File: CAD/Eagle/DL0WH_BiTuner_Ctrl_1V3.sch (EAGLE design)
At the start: 159 parts, among them Q0321 ABS07-32.768KHZ, U0101 STM32L476RGT6_64PIN_LDO, U0601 MC33996, U0701 MC33996, U0801 MC33996, U0921 TS5A23166, U0941 LM2611, U0951 OPA354, U0961 OPA354, U0962 MCP4661-103E-MS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

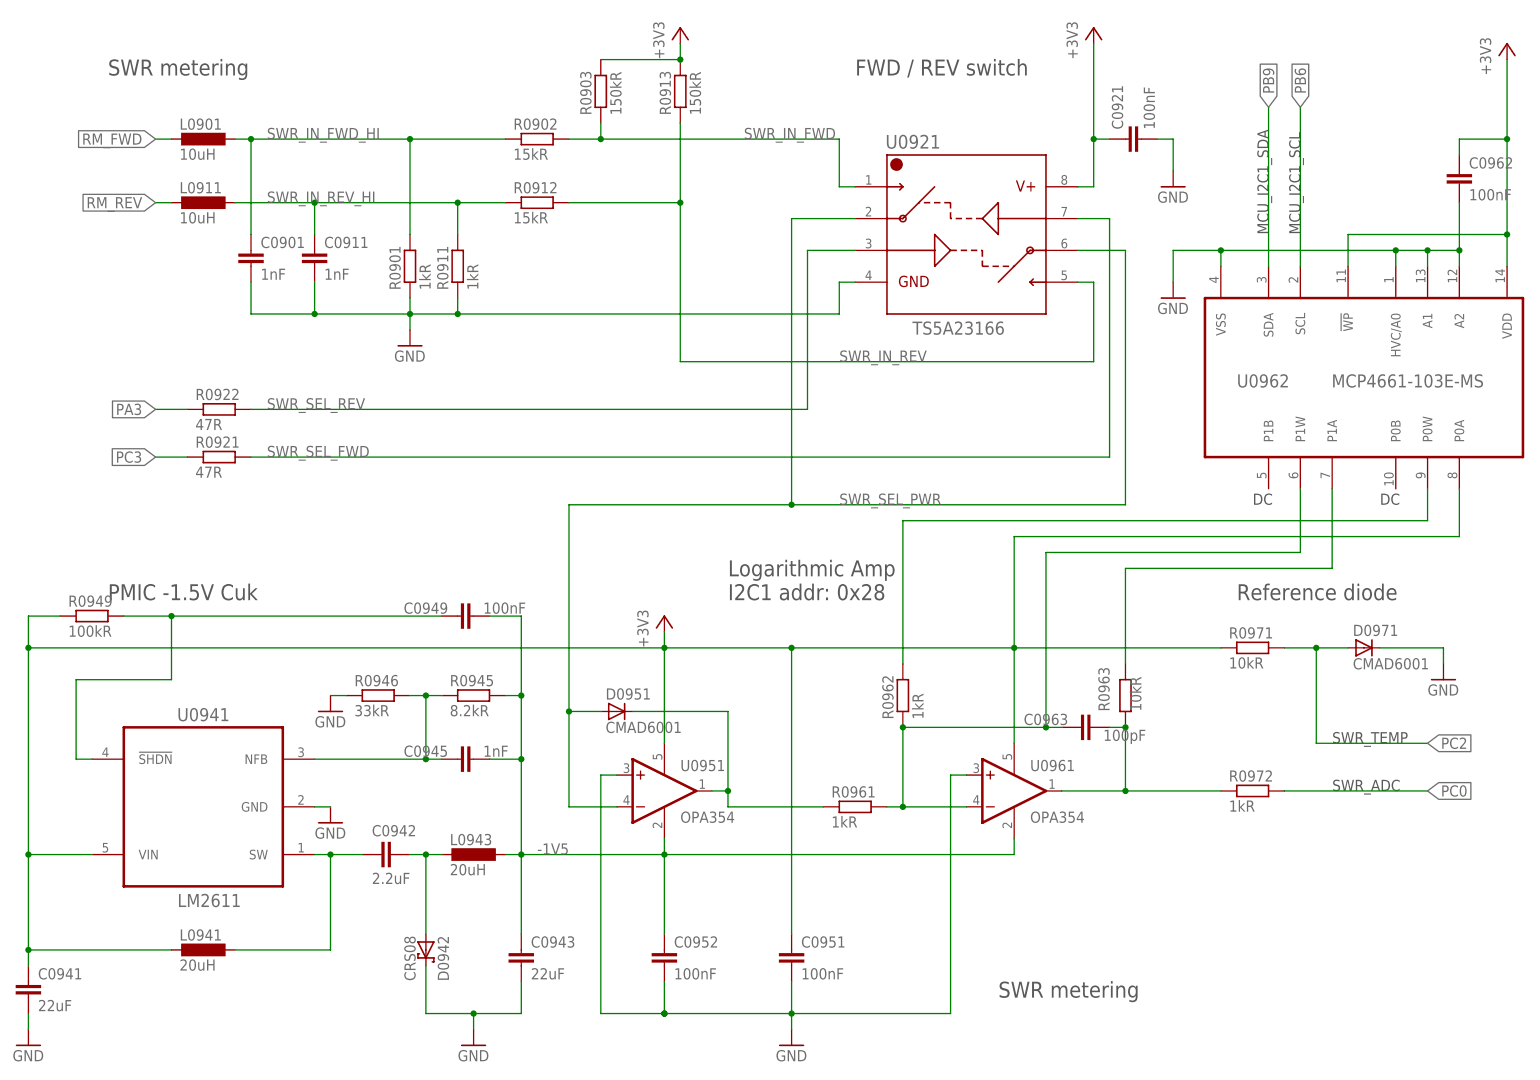
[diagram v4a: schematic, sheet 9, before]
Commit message: HW_1V3 - CAD/Eagle - soft-start not neded, prog. potis nominal values added
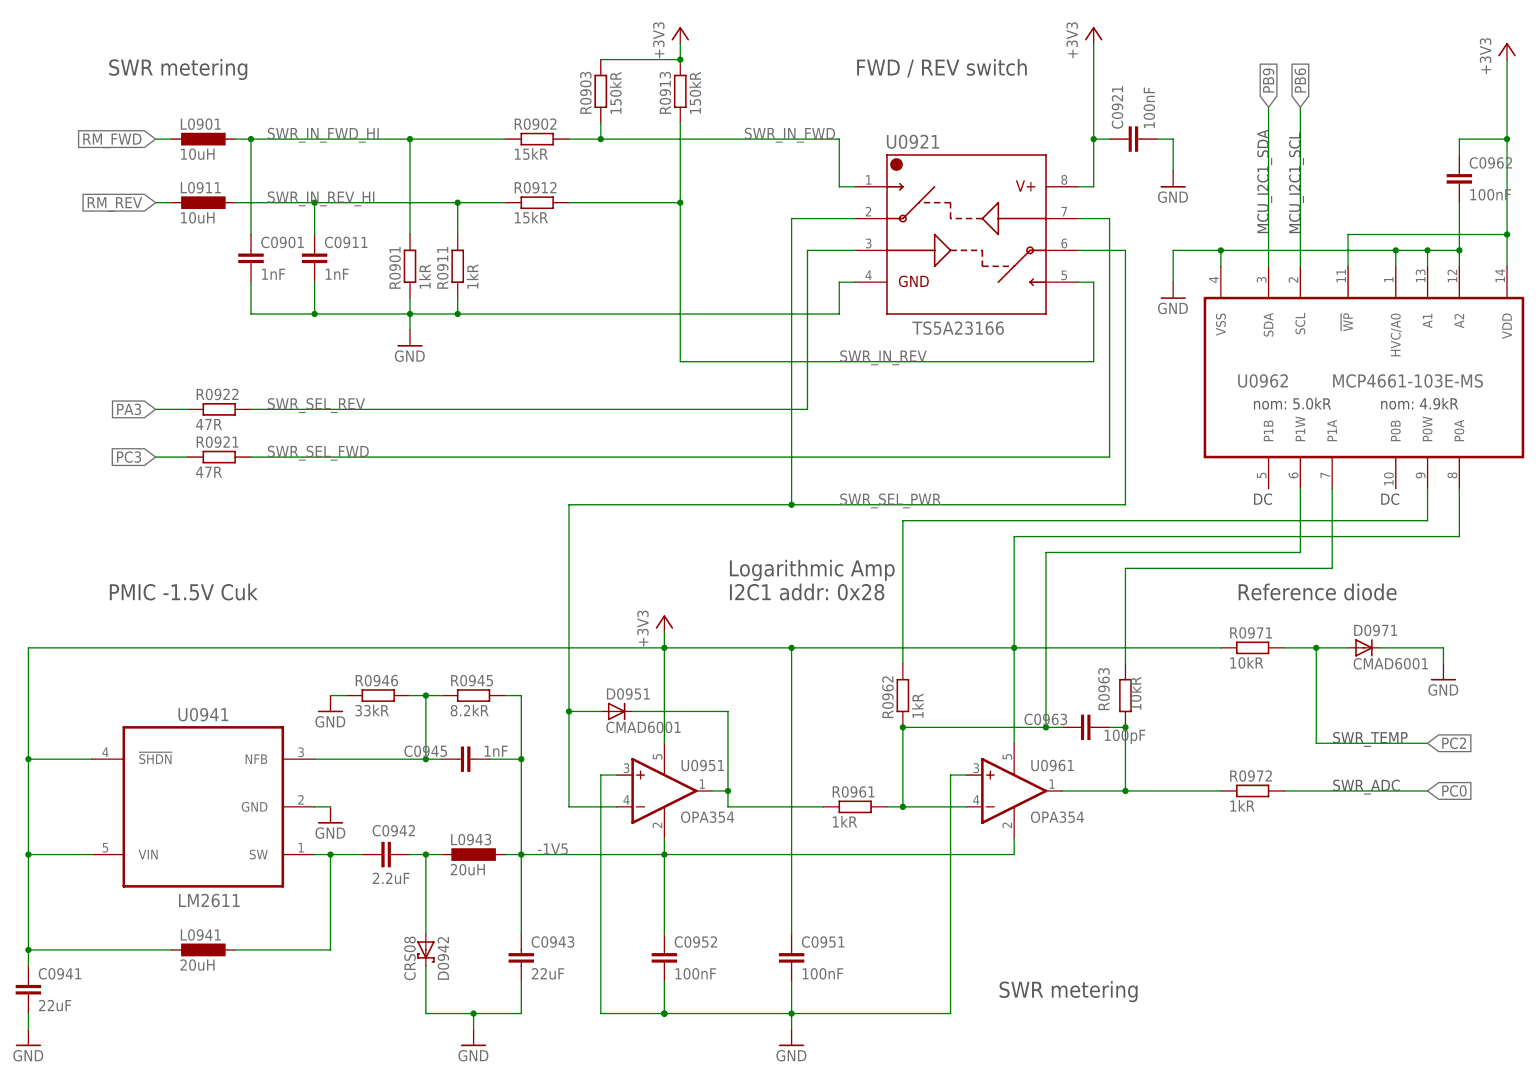
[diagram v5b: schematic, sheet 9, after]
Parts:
- removed C0949: 100nF, df4iah_rcl:C-EUC0402
- removed R0949: 100kR, df4iah_rcl:R-EU_R0402
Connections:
- removed net LM_SHDN: C0949.1, R0949.2, U0941.!SHDN
- net +3V3: now also U0941.!SHDN; no longer R0949.1
- net -1V5: no longer C0949.2
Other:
- note added: "nom: 4.9kR"
- note added: "nom: 5.0kR"
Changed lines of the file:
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@@
 <part name="+3V7" library="df4iah_supply" deviceset="+3V3" device=""/>
 <part name="C0962" library="df4iah_rcl" deviceset="C-EU" device="C0402" value="100nF"/>
-<part name="C0949" library="df4iah_rcl" deviceset="C-EU" device="C0402" value="100nF"/>
-<part name="R0949" library="df4iah_rcl" deviceset="R-EU_" device="R0402" value="100kR"/>
 </parts>
 <sheets>
@@
 <text x="213.36" y="137.16" size="1.778" layer="97" rot="R90">MCU_I2C1_SCL</text>
 <text x="208.28" y="137.16" size="1.778" layer="97" rot="R90">MCU_I2C1_SDA</text>
+<text x="205.74" y="109.22" size="1.778" layer="97">nom: 5.0kR</text>
+<text x="226.06" y="109.22" size="1.778" layer="97">nom: 4.9kR</text>
 </plain>
 <instances>
@@
 <instance part="+3V7" gate="G$1" x="246.38" y="167.64"/>
 <instance part="C0962" gate="G$1" x="238.76" y="147.32"/>
-<instance part="C0949" gate="G$1" x="78.74" y="76.2" smashed="yes" rot="R90">
-<attribute name="NAME" x="70.104" y="76.581" size="1.778" layer="95"/>
-<attribute name="VALUE" x="82.804" y="76.581" size="1.778" layer="96"/>
-</instance>
-<instance part="R0949" gate="G$1" x="20.32" y="76.2"/>
 </instances>
 <busses>
@@
 <pinref part="U0941" gate="G$1" pin="VIN"/>
 <wire x1="20.32" y1="38.1" x2="10.16" y2="38.1" width="0.1524" layer="91"/>
-<wire x1="10.16" y1="71.12" x2="10.16" y2="38.1" width="0.1524" layer="91"/>
+<wire x1="10.16" y1="71.12" x2="10.16" y2="53.34" width="0.1524" layer="91"/>
 <pinref part="C0941" gate="G$1" pin="1"/>
+<wire x1="10.16" y1="53.34" x2="10.16" y2="38.1" width="0.1524" layer="91"/>
 <wire x1="10.16" y1="38.1" x2="10.16" y2="22.86" width="0.1524" layer="91"/>
 <junction x="10.16" y="38.1"/>
@@
 <pinref part="U0962" gate="G$1" pin="P0A"/>
 <wire x1="238.76" y1="88.9" x2="238.76" y2="96.52" width="0.1524" layer="91"/>
-<wire x1="10.16" y1="71.12" x2="10.16" y2="76.2" width="0.1524" layer="91"/>
-<junction x="10.16" y="71.12"/>
-<pinref part="R0949" gate="G$1" pin="1"/>
-<wire x1="10.16" y1="76.2" x2="15.24" y2="76.2" width="0.1524" layer="91"/>
+<pinref part="U0941" gate="G$1" pin="!SHDN"/>
+<wire x1="10.16" y1="53.34" x2="20.32" y2="53.34" width="0.1524" layer="91"/>
+<junction x="10.16" y="53.34"/>
 </segment>
 <segment>
@@
 <wire x1="88.9" y1="53.34" x2="83.82" y2="53.34" width="0.1524" layer="91"/>
 <junction x="88.9" y="53.34"/>
-<wire x1="88.9" y1="63.5" x2="88.9" y2="76.2" width="0.1524" layer="91"/>
-<junction x="88.9" y="63.5"/>
-<pinref part="C0949" gate="G$1" pin="2"/>
-<wire x1="88.9" y1="76.2" x2="83.82" y2="76.2" width="0.1524" layer="91"/>
 </segment>
 </net>
@@
 </segment>
 </net>
-<net name="LM_SHDN" class="0">
-<segment>
-<pinref part="U0941" gate="G$1" pin="!SHDN"/>
-<wire x1="20.32" y1="53.34" x2="17.78" y2="53.34" width="0.1524" layer="91"/>
-<wire x1="17.78" y1="53.34" x2="17.78" y2="66.04" width="0.1524" layer="91"/>
-<wire x1="17.78" y1="66.04" x2="33.02" y2="66.04" width="0.1524" layer="91"/>
-<wire x1="33.02" y1="66.04" x2="33.02" y2="76.2" width="0.1524" layer="91"/>
-<pinref part="R0949" gate="G$1" pin="2"/>
-<wire x1="33.02" y1="76.2" x2="25.4" y2="76.2" width="0.1524" layer="91"/>
-<pinref part="C0949" gate="G$1" pin="1"/>
-<wire x1="33.02" y1="76.2" x2="76.2" y2="76.2" width="0.1524" layer="91"/>
-<junction x="33.02" y="76.2"/>
-</segment>
-</net>

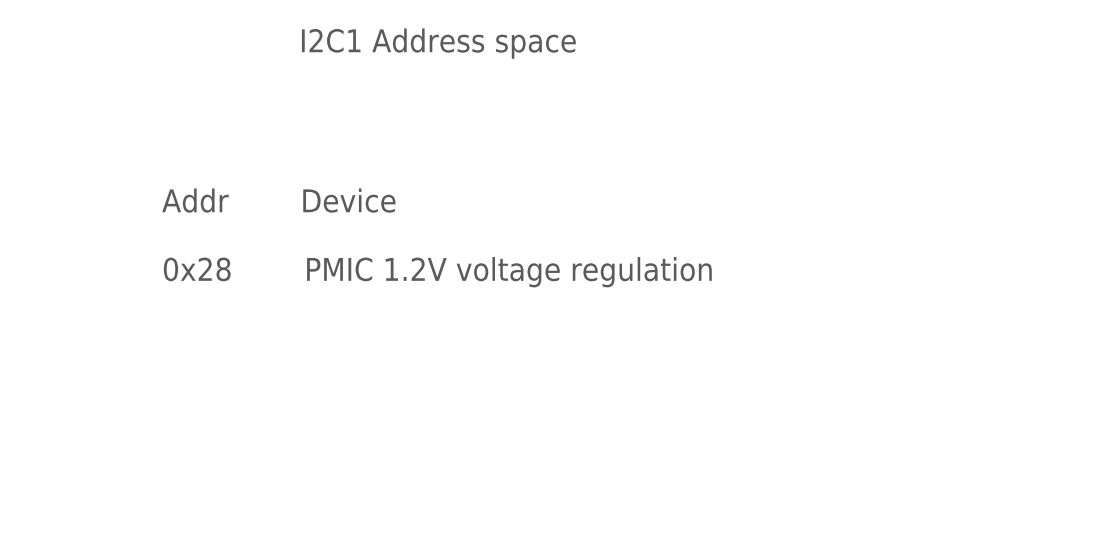
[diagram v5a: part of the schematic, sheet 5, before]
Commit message: HW_1V3 - CAD/Eagle - I2C address of dig.poti fixed to 0x14
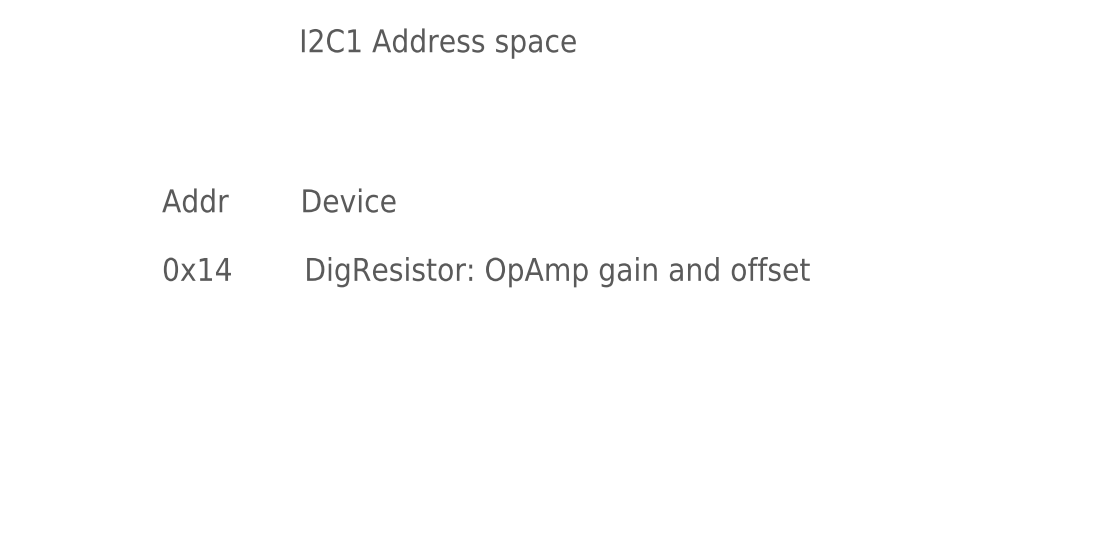
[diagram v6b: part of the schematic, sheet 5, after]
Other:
- note added: "Addr Device 0x14 DigResistor: OpAmp gain and offset"
- note removed: "Addr Device 0x28 PMIC 1.2V voltage regulation"
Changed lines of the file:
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@@
 <plain>
 <text x="134.62" y="137.16" size="2.54" layer="97" ratio="15">Addr        Device
-0x28        PMIC 1.2V voltage regulation
+0x14        DigResistor: OpAmp gain and offset
 </text>
 <text x="22.86" y="162.56" size="2.54" layer="97" ratio="15">I2C1 Termination</text>

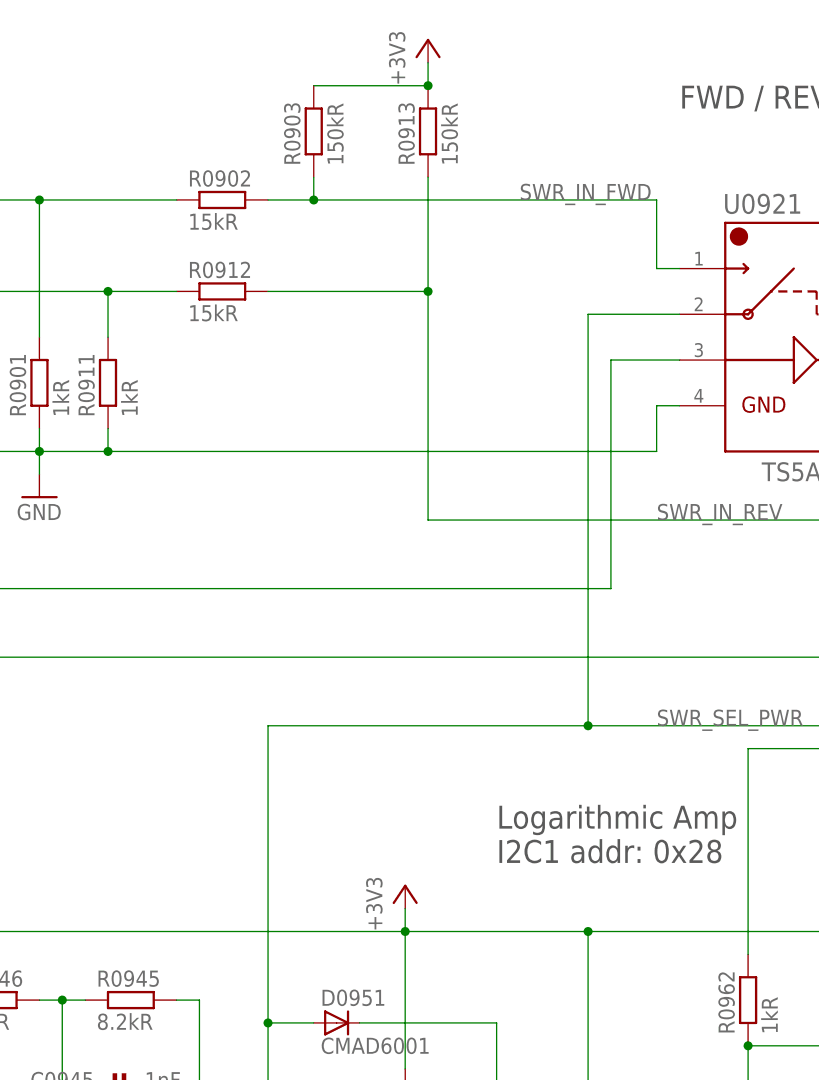
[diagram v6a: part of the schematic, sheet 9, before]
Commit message: HW_1V3 - CAD/Eagle - minor fixes for measurement unit to work
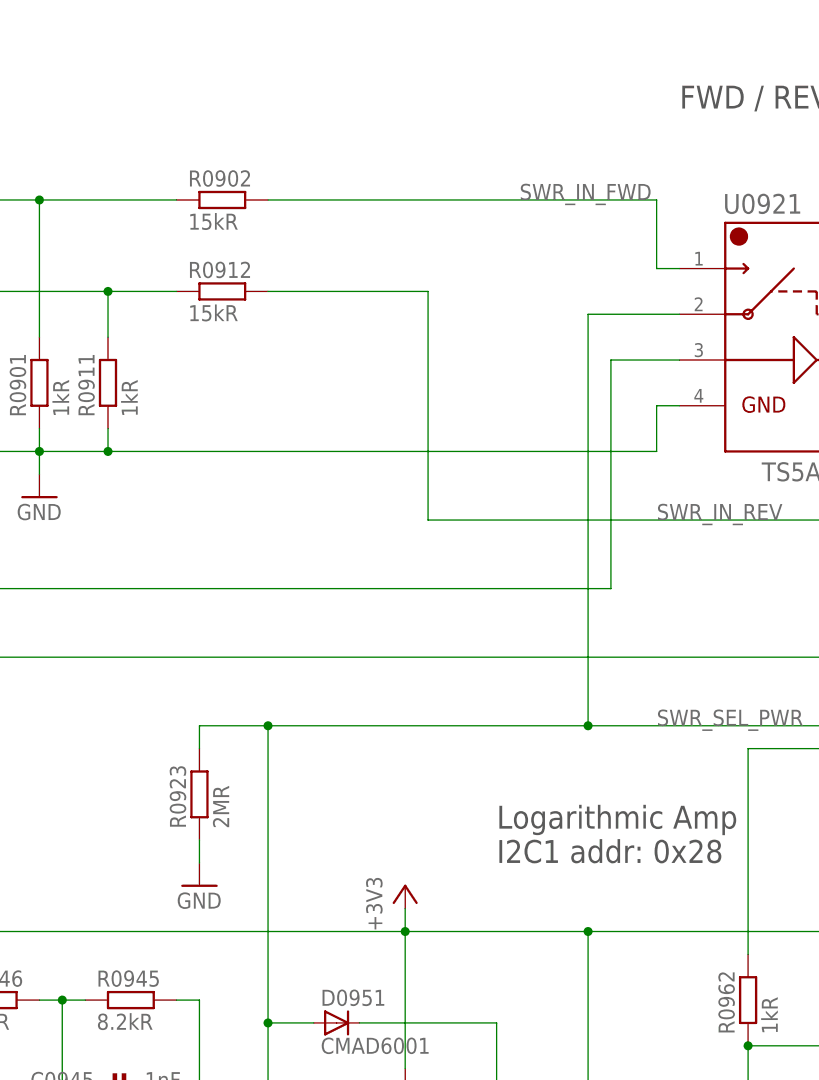
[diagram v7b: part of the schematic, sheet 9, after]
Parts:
- removed R0903, R0913: 150kR, df4iah_rcl:R-EU_R0402
- added R0923: 2MR, df4iah_rcl:R-EU_R0402
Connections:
- net +3V3: no longer R0903.2, R0913.2
- net GND: now also R0923.1
- net SWR_IN_FWD: no longer R0903.1
- net SWR_IN_REV: no longer R0913.1
- net SWR_SEL_PWR: now also R0923.2
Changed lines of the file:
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@@
 <part name="X0501" library="df4iah_connector" deviceset="HEADER-2X2" device=""/>
 <part name="GND0501" library="df4iah_supply" deviceset="GND" device=""/>
-<part name="+3V6" library="df4iah_supply" deviceset="+3V3" device=""/>
-<part name="R0903" library="df4iah_rcl" deviceset="R-EU_" device="R0402" value="150kR"/>
-<part name="R0913" library="df4iah_rcl" deviceset="R-EU_" device="R0402" value="150kR"/>
 <part name="R0901" library="df4iah_rcl" deviceset="R-EU_" device="R0402" value="1kR"/>
 <part name="R0911" library="df4iah_rcl" deviceset="R-EU_" device="R0402" value="1kR"/>
@@
 <part name="+3V7" library="df4iah_supply" deviceset="+3V3" device=""/>
 <part name="C0962" library="df4iah_rcl" deviceset="C-EU" device="C0402" value="100nF"/>
+<part name="R0923" library="df4iah_rcl" deviceset="R-EU_" device="R0402" value="2MR"/>
+<part name="GND0922" library="df4iah_supply" deviceset="GND" device=""/>
 </parts>
 <sheets>
@@
 <instance part="R0971" gate="G$1" x="205.74" y="71.12"/>
 <instance part="GND0961" gate="1" x="236.22" y="66.04"/>
-<instance part="+3V6" gate="G$1" x="114.3" y="170.18"/>
-<instance part="R0903" gate="G$1" x="101.6" y="160.02" rot="R90"/>
-<instance part="R0913" gate="G$1" x="114.3" y="160.02" rot="R90"/>
 <instance part="R0901" gate="G$1" x="71.12" y="132.08" rot="R90"/>
 <instance part="R0911" gate="G$1" x="78.74" y="132.08" rot="R90"/>
@@
 <instance part="+3V7" gate="G$1" x="246.38" y="167.64"/>
 <instance part="C0962" gate="G$1" x="238.76" y="147.32"/>
+<instance part="R0923" gate="G$1" x="88.9" y="86.36" rot="R90"/>
+<instance part="GND0922" gate="1" x="88.9" y="76.2"/>
 </instances>
 <busses>
@@
 <pinref part="R0912" gate="G$1" pin="2"/>
 <label x="139.7" y="116.84" size="1.778" layer="95"/>
-<junction x="114.3" y="142.24"/>
-<pinref part="R0913" gate="G$1" pin="1"/>
-<wire x1="114.3" y1="154.94" x2="114.3" y2="142.24" width="0.1524" layer="91"/>
 </segment>
 </net>
@@
 <wire x1="139.7" y1="144.78" x2="142.24" y2="144.78" width="0.1524" layer="91"/>
 <pinref part="R0902" gate="G$1" pin="2"/>
-<wire x1="139.7" y1="152.4" x2="101.6" y2="152.4" width="0.1524" layer="91"/>
+<wire x1="139.7" y1="152.4" x2="96.52" y2="152.4" width="0.1524" layer="91"/>
 <label x="124.46" y="152.4" size="1.778" layer="95"/>
-<wire x1="101.6" y1="152.4" x2="96.52" y2="152.4" width="0.1524" layer="91"/>
-<pinref part="R0903" gate="G$1" pin="1"/>
-<wire x1="101.6" y1="152.4" x2="101.6" y2="154.94" width="0.1524" layer="91"/>
-<junction x="101.6" y="152.4"/>
 </segment>
 </net>
@@
 <wire x1="238.76" y1="134.62" x2="238.76" y2="142.24" width="0.1524" layer="91"/>
 <junction x="238.76" y="134.62"/>
+</segment>
+<segment>
+<pinref part="GND0922" gate="1" pin="GND"/>
+<pinref part="R0923" gate="G$1" pin="1"/>
+<wire x1="88.9" y1="78.74" x2="88.9" y2="81.28" width="0.1524" layer="91"/>
 </segment>
 </net>
@@
 </segment>
 <segment>
-<wire x1="114.3" y1="165.1" x2="114.3" y2="167.64" width="0.1524" layer="91"/>
-<junction x="114.3" y="165.1"/>
-<pinref part="+3V6" gate="G$1" pin="+3V3"/>
-<pinref part="R0913" gate="G$1" pin="2"/>
-<pinref part="R0903" gate="G$1" pin="2"/>
-<wire x1="114.3" y1="165.1" x2="101.6" y2="165.1" width="0.1524" layer="91"/>
-</segment>
-<segment>
 <pinref part="U0962" gate="G$1" pin="VDD"/>
 <wire x1="246.38" y1="132.08" x2="246.38" y2="137.16" width="0.1524" layer="91"/>
@@
 <wire x1="96.52" y1="60.96" x2="101.6" y2="60.96" width="0.1524" layer="91"/>
 <junction x="96.52" y="60.96"/>
-</segment>
-</net>
+<wire x1="96.52" y1="93.98" x2="88.9" y2="93.98" width="0.1524" layer="91"/>
+<junction x="96.52" y="93.98"/>
+<pinref part="R0923" gate="G$1" pin="2"/>
+<wire x1="88.9" y1="93.98" x2="88.9" y2="91.44" width="0.1524" layer="91"/>
+</segment>
+</net>
